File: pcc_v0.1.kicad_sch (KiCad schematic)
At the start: 56 parts, among them K1 Gigavac GV242BAB, K2 CPC1706, Q1 BS108, Q2 BS108, U2 4N35, U3 4N35, U5 TJA1051T-3, U7 Teensy4.0

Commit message: pcc modifications
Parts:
- removed 100n1, 100n2: C, symbol Device:C
- removed D1, D2: D, symbol Device:D
- removed R27, R28: 150K, symbol Device:R_US
- removed R29: 120, symbol Device:R_Small_US
- removed R30, R31: 160, symbol Device:R_Small_US
- removed U5: TJA1051T-3, Package_SO:SOIC-8_3.9x4.9mm_P1.27mm, symbol Interface_CAN_LIN:TJA1051T-3
- added R27: 120, Resistor_SMD:R_0805_2012Metric, symbol Device:R_Small_US
- added U8: SN65HVD230, Package_SO:SOIC-8_3.9x4.9mm_P1.27mm, symbol Interface_CAN_LIN:SN65HVD230
- C1, C2, C3, C4, C5, C6, C7, C8, C9: footprint (none) -> Capacitor_SMD:C_0805_2012Metric
- R1, R2, R21, R23, R24, R25, R3, R4, R5: value 150K -> 510K; footprint (none) -> Resistor_SMD:R_0805_2012Metric
- R10, R11, R12, R13, R14, R15, R16, R17, R18, R19, R26, R32, R7, R8, R9: footprint (none) -> Resistor_SMD:R_0805_2012Metric
- R20: value 150K -> 39K; footprint (none) -> Resistor_SMD:R_0805_2012Metric
- R22: value 100K -> 510K; footprint (none) -> Resistor_SMD:R_0805_2012Metric
- R6: value 100K -> 39K; footprint (none) -> Resistor_SMD:R_0805_2012Metric
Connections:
- net +3.3V: now also U8.3 (VCC)
- net CANH: now also R27.1, U8.7 (CANH)
- net CANRX: now also U8.4 (R)
- net CANTX: now also U8.1 (D)
- net GLV-: now also U8.2 (GND), U8.8 (Rs)
- net GNDS: now also R20.2; no longer R22.2
- net Vin_TS: now also R21.1; no longer R23.1
- net at R6.1, R7.2: now also R4.2; no longer R5.2
- net at R21.2, R22.1: no longer R19.2
- net at R20.1: now also R19.2, R5.2
- net at R5.1: now also R24.2; no longer R4.2
- net Error: no longer names the net of U7.5 (3_LRCLK2)
- net Online: no longer names the net of U7.4 (2_OUT2)
- net Precharge: no longer names the net of U7.3 (1_TX1_CTX2_MISO1)
- net Standby: no longer names the net of U7.2 (0_RX1_CRX2_CS1)
- new net: R27.2, U8.6 (CANL)
- new net: R22.2, R23.1
- no-connect marks 2 -> 3

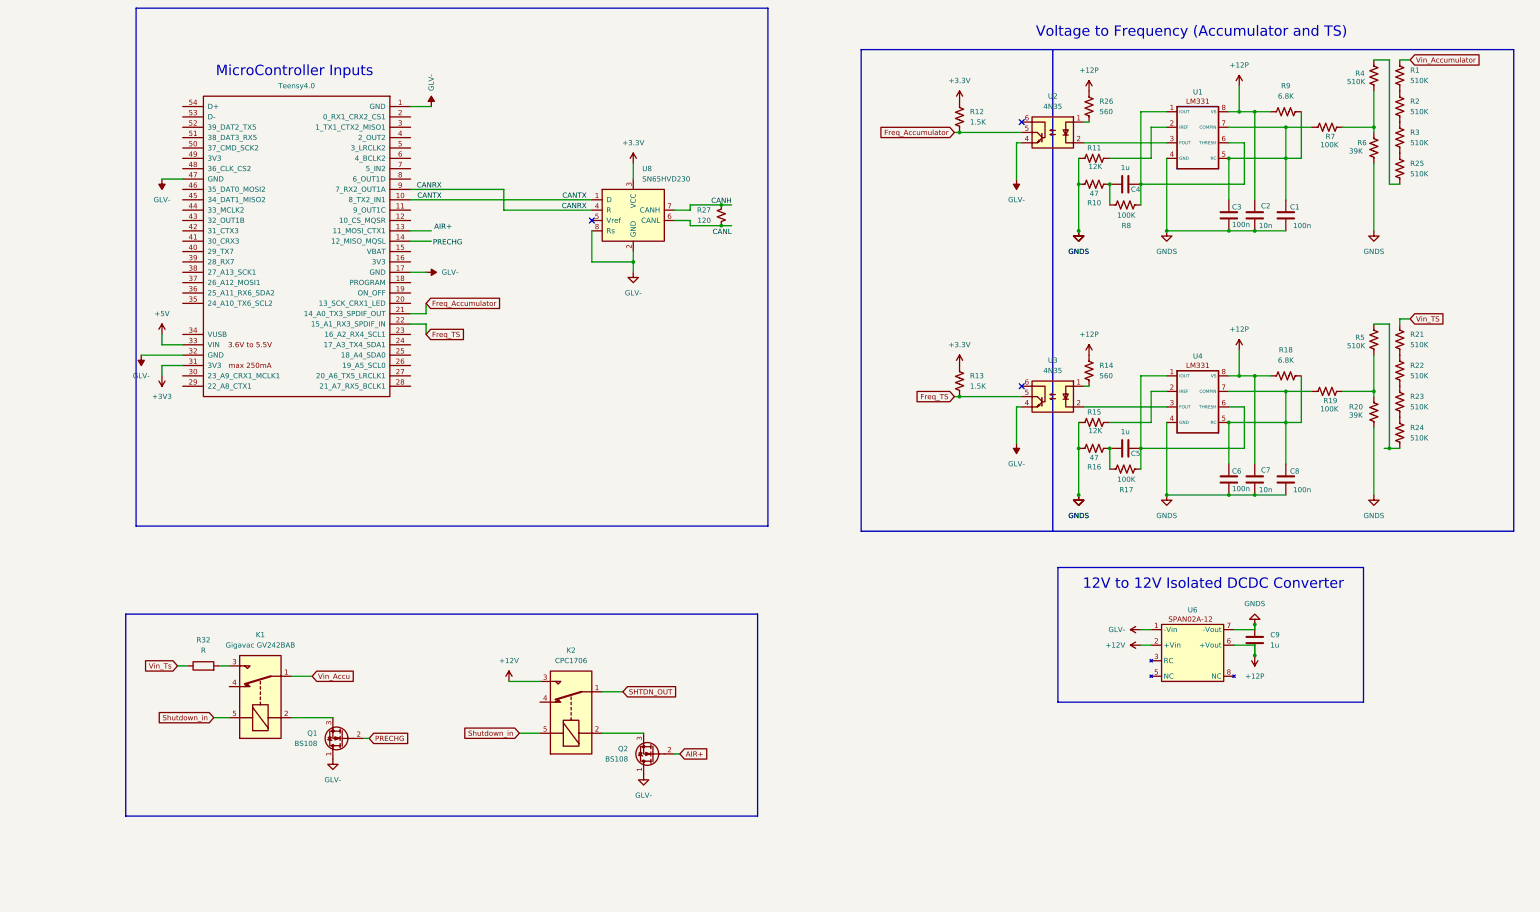
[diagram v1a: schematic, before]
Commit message: started pcb layout
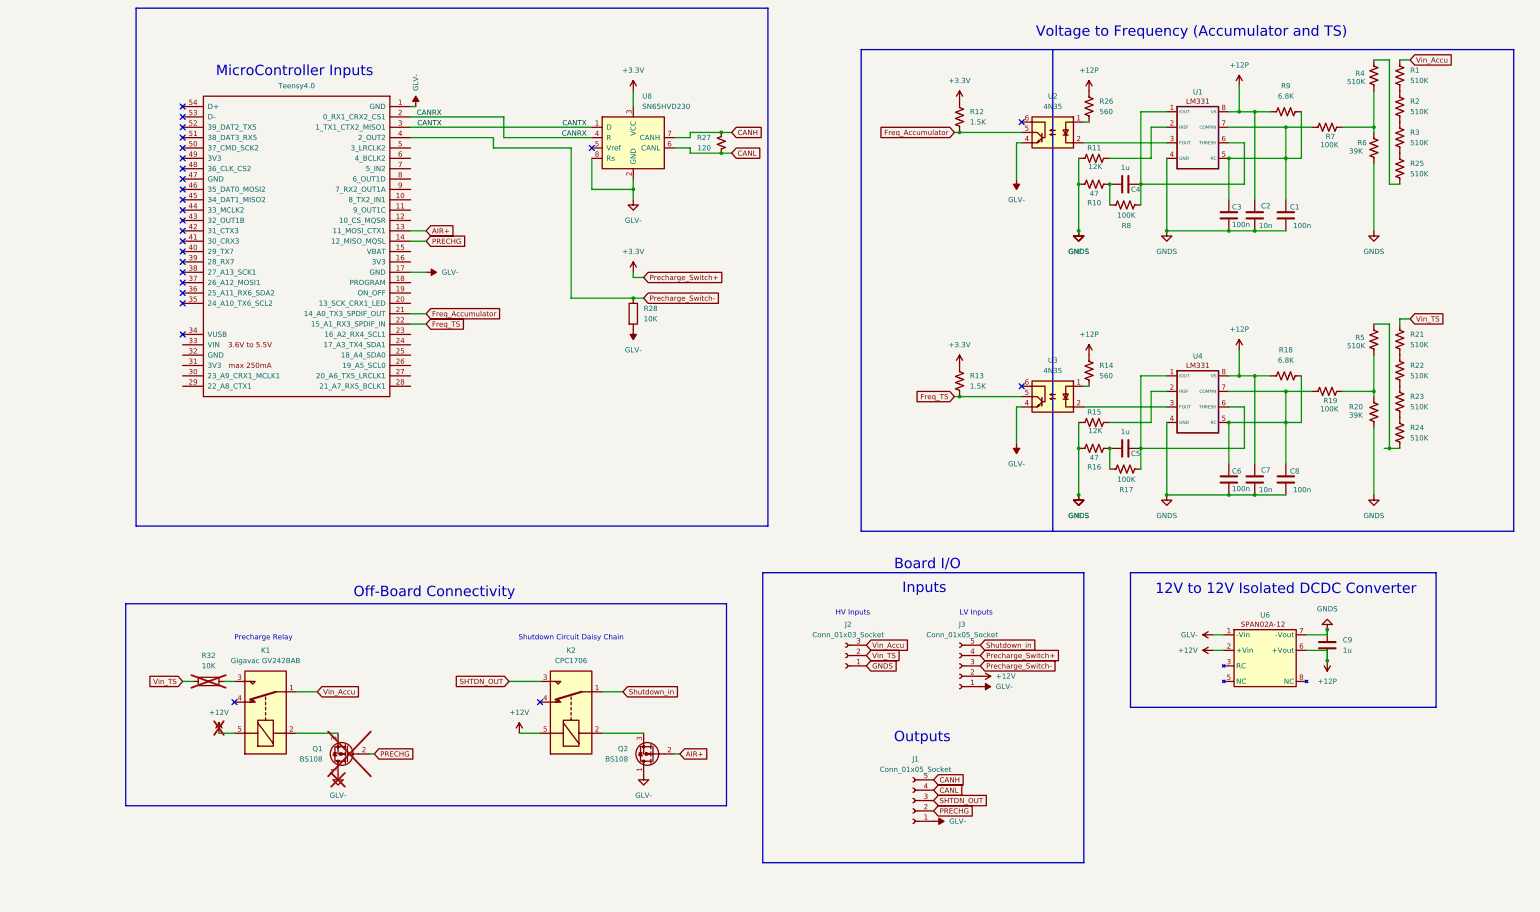
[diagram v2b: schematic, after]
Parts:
- added J1, J3: Conn_01x05_Socket, Connector_Molex:Molex_Micro-Fit_3.0_43045-0612_2x03_P3.00mm_Vertical, symbol Connector:Conn_01x05_Socket
- added J2: Conn_01x03_Socket, Connector_Molex:Molex_Micro-Fit_3.0_43650-0315_1x03_P3.00mm_Vertical, symbol Connector:Conn_01x03_Socket
- added R28: 10K, Resistor_SMD:R_0805_2012Metric, symbol Device:R
- Q1: now not fitted
- R32: value R -> 10K; now not fitted
- U1, U4: footprint (none) -> Package_DIP:DIP-8_W7.62mm_Socket
- U2, U3: footprint Package_DIP:DIP-6_W7.62mm -> Package_DIP:DIP-6_W7.62mm_Socket
- U6: footprint (none) -> Package_SIP:SIP-8_19x3mm_P2.54mm
- U7: footprint (none) -> Package_DIP:DIP-28_W15.24mm_Socket
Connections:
- net Vin_Accumulator is gone; now on net Vin_Accu: R1.1
- net Vin_Ts is gone; now on net Vin_TS: R32.1
- net +12V: now also K1.5, K2.5, J3.2 (Pin_2); no longer K2.3
- net +3.3V: now also J3.4 (Pin_4)
- net AIR+: now also U7.13 (11_MOSI_CTX1)
- net CANH: now also J1.5 (Pin_5)
- net CANL: now also R27.2, U8.6 (CANL), J1.4 (Pin_4)
- net CANRX: now also U7.2 (0_RX1_CRX2_CS1); no longer U7.9 (7_RX2_OUT1A)
- net CANTX: now also U7.3 (1_TX1_CTX2_MISO1); no longer U7.10 (8_TX2_IN1)
- net GLV-: now also J1.1 (Pin_1), J3.1 (Pin_1), R28.2; no longer U7.32 (GND), U7.47 (GND)
- net GNDS: now also J2.1 (Pin_1)
- net PRECHG: now also U7.14 (12_MISO_MQSL), J1.2 (Pin_2)
- net SHTDN_OUT: now also K2.3, J1.3 (Pin_3); no longer K2.1
- net Shutdown_in: now also K2.1, J3.5 (Pin_5); no longer K1.5, K2.5
- net Vin_Accu: now also J2.3 (Pin_3)
- net Vin_TS: now also J2.2 (Pin_2)
- net Precharge_Switch-: now reaches U7.4 (2_OUT2)
- net Precharge_Switch-: now also J3.3 (Pin_3), R28.1
- net +3V3: no longer names the net of U7.31 (3V3)
- net +5V: no longer names the net of U7.33 (VIN)
- no-connect marks 3 -> 26
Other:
- note added: "Board I/O"
- note added: "HV Inputs"
- note added: "Inputs"
- note added: "LV Inputs"
- note added: "Off-Board Connectivity"
- note added: "Outputs"
- note added: "Precharge Relay"
- note added: "Shutdown Circuit Daisy Chain"
- moved on the sheet: C9, K1, R27, U6, U8

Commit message: polishing layout
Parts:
- removed R28: 10K, Resistor_SMD:R_0805_2012Metric, symbol Device:R
- added J4: Conn_02x14_Counter_Clockwise, Package_DIP:DIP-28_W15.24mm_Socket, symbol Connector_Generic:Conn_02x14_Counter_Clockwise
- C2, C7: value 10n -> 100n
- C3, C6: value 100n -> 10n
- Q1, R32: now fitted
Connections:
- net +3.3V: now also U7.31 (3V3), J4.26 (Pin_26)
- net AIR+: now also J4.13 (Pin_13)
- net CANRX: now also J4.2 (Pin_2)
- net CANTX: now also J4.3 (Pin_3)
- net Freq_Accumulator: now also J4.16 (Pin_16)
- net Freq_TS: now also J4.17 (Pin_17)
- net GLV-: now also U7.32 (GND), J4.1 (Pin_1), J4.27 (Pin_27)
- net PRECHG: now also J4.14 (Pin_14)
- net Precharge_Switch-: now also J4.4 (Pin_4)
- net at C6.1, R18.2, U4.5 (RC): no longer C8.1, R19.1, U4.7 (COMPIN)
- net at C1.1, R7.1, U1.7 (COMPIN): no longer C3.1, R9.2, U1.5 (RC)
- net +5V: now reaches U7.33 (VIN)
- net +5V: now also J4.28 (Pin_28)
- new net: C8.1, R19.1, U4.7 (COMPIN)
- new net: C3.1, R9.2, U1.5 (RC)
- no-connect marks 26 -> 47

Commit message: cleaned up layout
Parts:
- removed J1, J3: Conn_01x05_Socket, Connector_Molex:Molex_Micro-Fit_3.0_43045-0612_2x03_P3.00mm_Vertical, symbol Connector:Conn_01x05_Socket
- removed J2: Conn_01x03_Socket, Connector_Molex:Molex_Micro-Fit_3.0_43650-0315_1x03_P3.00mm_Vertical, symbol Connector:Conn_01x03_Socket
- added J1: Conn_01x04_Socket, Connector_Molex:Molex_Mini-Fit_Jr_5566-04A2_2x02_P4.20mm_Vertical, symbol Connector:Conn_01x04_Socket
- added J5, J6: Conn_01x06_Socket, Connector_Molex:Molex_Mini-Fit_Jr_5566-06A2_2x03_P4.20mm_Vertical, symbol Connector:Conn_01x06_Socket
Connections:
- net +12V: now also J5.2 (Pin_2)
- net +3.3V: now also J5.4 (Pin_4)
- net CANH: now also J6.5 (Pin_5)
- net CANL: now also J6.4 (Pin_4)
- net GLV-: now also J5.1 (Pin_1), J6.1 (Pin_1)
- net GNDS: now also J1.1 (Pin_1)
- net PRECHG: now also J6.2 (Pin_2)
- net Precharge_Switch-: now also J5.3 (Pin_3)
- net SHTDN_OUT: now also J6.3 (Pin_3)
- net Shutdown_in: now also J5.5 (Pin_5)
- net Vin_Accu: now also J1.4 (Pin_4)
- net Vin_TS: now also J1.3 (Pin_3)
- no-connect marks 47 -> 50

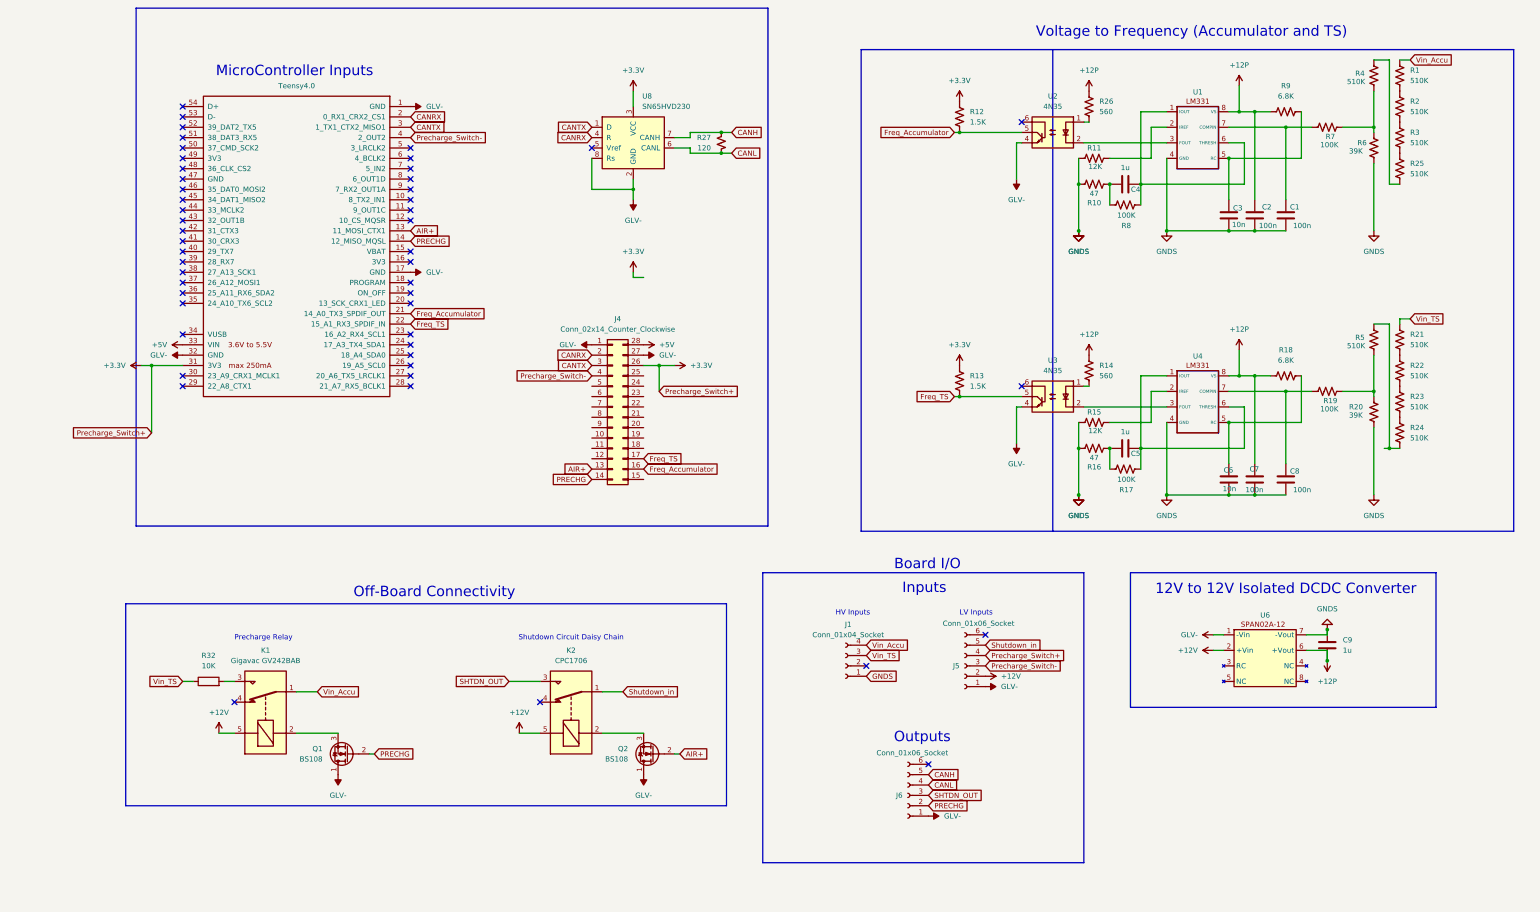
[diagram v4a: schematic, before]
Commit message: revised with all relay outputs
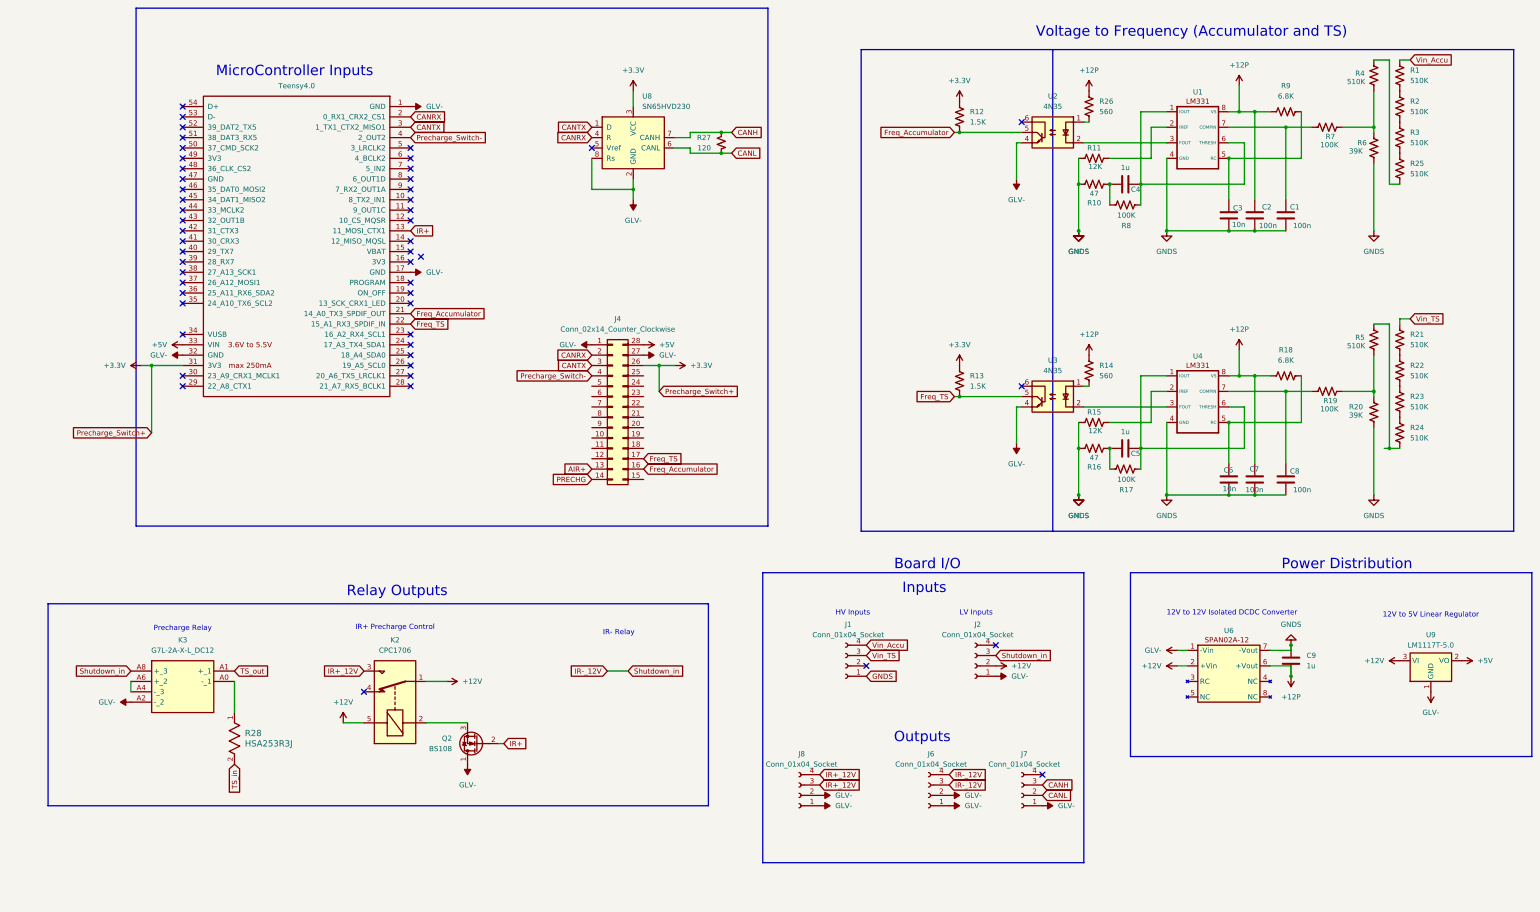
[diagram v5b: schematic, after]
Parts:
- removed J5, J6: Conn_01x06_Socket, Connector_Molex:Molex_Mini-Fit_Jr_5566-06A2_2x03_P4.20mm_Vertical, symbol Connector:Conn_01x06_Socket
- removed K1: Gigavac GV242BAB, Relay_THT:Relay_SPDT_SANYOU_SRD_Series_Form_C, symbol Relay:SANYOU_SRD_Form_C
- removed Q1: BS108, Package_TO_SOT_THT:TO-92_Inline, symbol Transistor_FET:BS108
- removed R32: 10K, Resistor_SMD:R_0805_2012Metric, symbol Device:R
- added J2, J6, J7, J8: Conn_01x04_Socket, Connector_Molex:Molex_Mini-Fit_Jr_5566-04A2_2x02_P4.20mm_Vertical, symbol Connector:Conn_01x04_Socket
- added K3: G7L-2A-X-L_DC12, KiCad:G7L2AXLDC12, symbol G7L-2A-X-L_DC12:G7L-2A-X-L_DC12
- added R28: HSA253R3J, footprints:RES_HSA25_TYCO_TYC, symbol 2025-01-28_17-59-30:HSA253R3J
- added U9: LM1117T-5.0, Package_TO_SOT_THT:TO-220-3_Horizontal_TabDown, symbol Regulator_Linear:LM1117T-5.0
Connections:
- net Shutdown_in is gone; now on net +12V: K2.1
- net +12V: now also J2.2 (Pin_2), U9.3 (VI)
- net +5V: now also U9.2 (VO)
- net AIR+: no longer Q2.2 (G), U7.13 (11_MOSI_CTX1)
- net CANH: now also J7.3 (Pin_3)
- net CANL: now also J7.2 (Pin_2)
- net GLV-: now also J2.1 (Pin_1), J6.1 (Pin_1), J6.2 (Pin_2), J7.1 (Pin_1), J8.1 (Pin_1), J8.2 (Pin_2), K3.A2 (-_2), U9.1 (GND)
- net PRECHG: no longer U7.14 (12_MISO_MQSL)
- net SHTDN_OUT renamed IR+_12V
- net IR+_12V: now also J8.3 (Pin_3), J8.4 (Pin_4)
- new net: K3.A0 (-_1), R28.1
- new net: K3.A4 (-_3), K3.A6 (+_2)
- new net IR+: Q2.2 (G), U7.13 (11_MOSI_CTX1)
- new net IR-_12V: J2.3 (Pin_3), J6.3 (Pin_3), J6.4 (Pin_4), K3.A8 (+_3)
- new net TS_in: R28.2
- new net TS_out: K3.A1 (+_1)
- no-connect marks 50 -> 51
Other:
- note added: "12V to 5V Linear Regulator"
- note added: "IR+ Precharge Control"
- note added: "IR- Relay"
- note added: "Power Distribution"
- note added: "Relay Outputs"
- note removed: "Off-Board Connectivity"
- note removed: "Shutdown Circuit Daisy Chain"
- moved on the sheet: C9, K2, Q2, U6
